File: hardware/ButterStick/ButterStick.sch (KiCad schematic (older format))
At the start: 0 parts

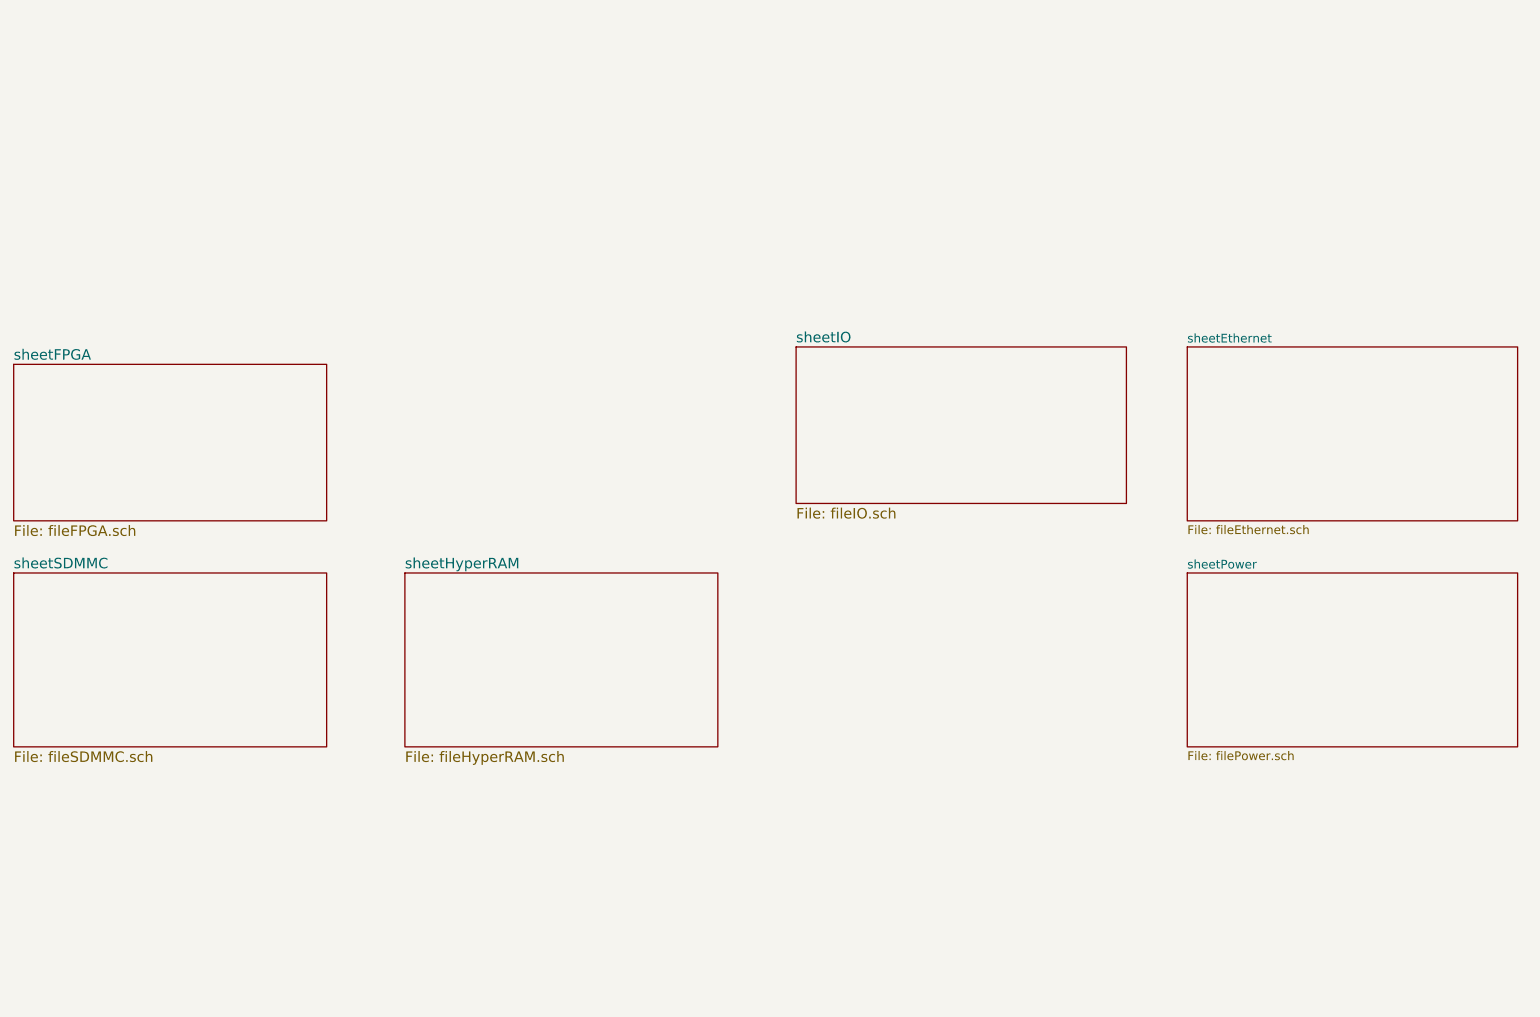
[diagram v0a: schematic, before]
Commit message: Update schematic hieracy layout.
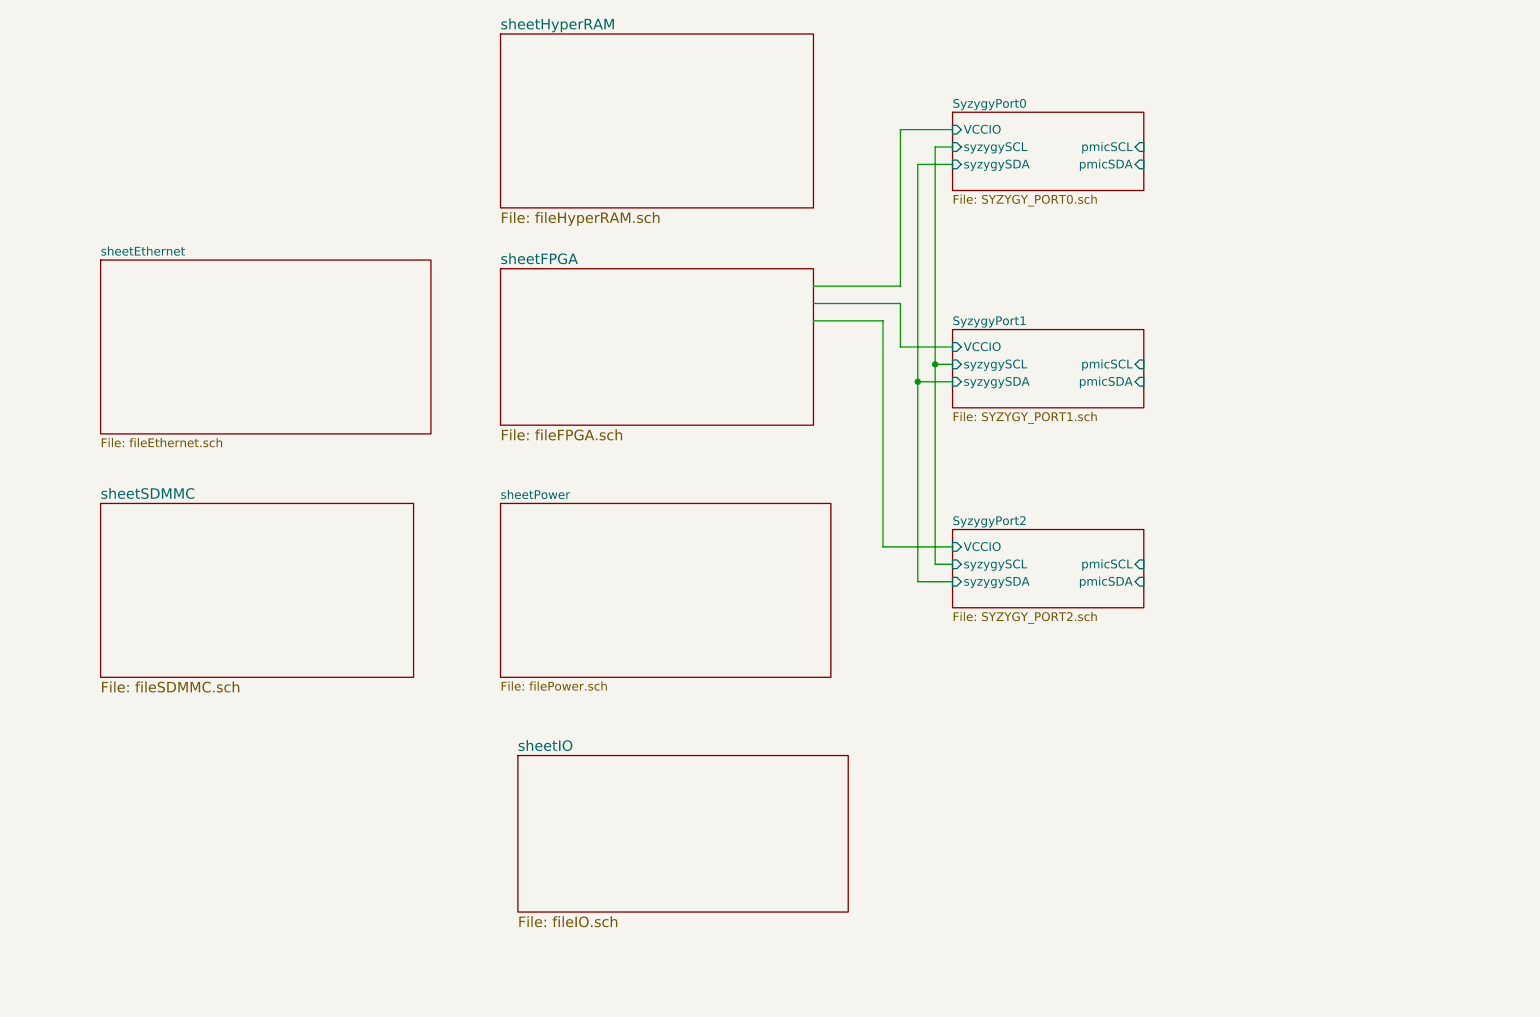
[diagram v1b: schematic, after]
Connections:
- wire segments 0 -> 19
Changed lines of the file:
@@
 $Descr A4 11693 8268
 encoding utf-8
-Sheet 1 7
+Sheet 1 13
 Title ""
 Date ""
@@
 $EndDescr
 $Sheet
-S 1800 3000 1800 900
+S 4600 2450 1800 900
 U 5AB8ACB7
 F0 "sheetFPGA" 60
@@
 $EndSheet
 $Sheet
-S 4050 4200 1800 1000
+S 4600 1100 1800 1000
 U 5ABD38F2
 F0 "sheetHyperRAM" 60
@@
 $EndSheet
 $Sheet
-S 1800 4200 1800 1000
+S 2300 3800 1800 1000
 U 5AC0A2A0
 F0 "sheetSDMMC" 60
@@
 $EndSheet
 $Sheet
-S 6300 2900 1900 900
+S 4700 5250 1900 900
 U 5ABC9A87
 F0 "sheetIO" 60
@@
 $EndSheet
 $Sheet
-S 8550 2900 1900 1000
+S 2300 2400 1900 1000
 U 5BA0BA35
 F0 "sheetEthernet" 50
@@
 $EndSheet
 $Sheet
-S 8550 4200 1900 1000
+S 4600 3800 1900 1000
 U 5BBD18EA
 F0 "sheetPower" 50
 F1 "filePower.sch" 50
 $EndSheet
+$Sheet
+S 7200 1550 1100 450
+U 5C80F19A
+F0 "SyzygyPort0" 50
+F1 "SYZYGY_PORT0.sch" 50
+F2 "VCCIO" I L 7200 1650 50
+F3 "syzygySCL" I L 7200 1750 50
+F4 "syzygySDA" I L 7200 1850 50
+F5 "pmicSCL" I R 8300 1750 50
+F6 "pmicSDA" I R 8300 1850 50
+$EndSheet
+$Sheet
+S 7200 2800 1100 450
+U 5C80F19D
+F0 "SyzygyPort1" 50
+F1 "SYZYGY_PORT1.sch" 50
+F2 "VCCIO" I L 7200 2900 50
+F3 "syzygySCL" I L 7200 3000 50
+F4 "syzygySDA" I L 7200 3100 50
+F5 "pmicSCL" I R 8300 3000 50
+F6 "pmicSDA" I R 8300 3100 50
+$EndSheet
+$Sheet
+S 7200 3950 1100 450
+U 5C80F1A0
+F0 "SyzygyPort2" 50
+F1 "SYZYGY_PORT2.sch" 50
+F2 "VCCIO" I L 7200 4050 50
+F3 "syzygySCL" I L 7200 4150 50
+F4 "syzygySDA" I L 7200 4250 50
+F5 "pmicSCL" I R 8300 4150 50
+F6 "pmicSDA" I R 8300 4250 50
+$EndSheet
+Wire Wire Line
+	7200 4150 7100 4150
+Wire Wire Line
+	7100 4150 7100 3000
+Wire Wire Line
+	7100 1750 7200 1750
+Wire Wire Line
+	7200 1850 7000 1850
+Wire Wire Line
+	7000 1850 7000 3100
+Wire Wire Line
+	7000 4250 7200 4250
+Wire Wire Line
+	7200 3100 7000 3100
+Connection ~ 7000 3100
+Wire Wire Line
+	7000 3100 7000 4250
+Wire Wire Line
+	7200 3000 7100 3000
+Connection ~ 7100 3000
+Wire Wire Line
+	7100 3000 7100 1750
+Wire Wire Line
+	7200 1650 6900 1650
+Wire Wire Line
+	6900 1650 6900 2550
+Wire Wire Line
+	6900 2550 6400 2550
+Wire Wire Line
+	7200 2900 6900 2900
+Wire Wire Line
+	6900 2900 6900 2650
+Wire Wire Line
+	6900 2650 6400 2650
+Wire Wire Line
+	7200 4050 6800 4050
+Wire Wire Line
+	6800 4050 6800 2750
+Wire Wire Line
+	6800 2750 6400 2750
 $EndSCHEMATC

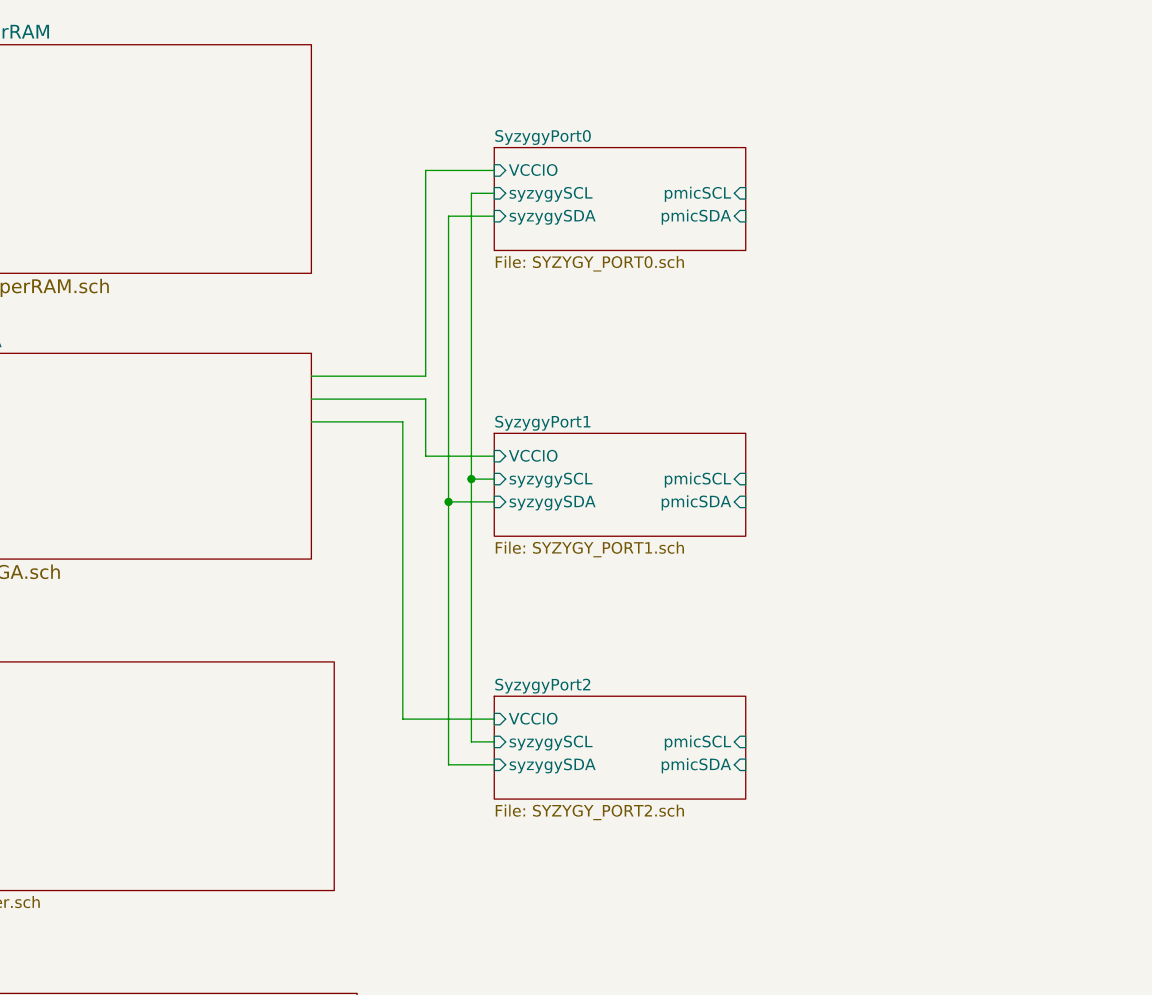
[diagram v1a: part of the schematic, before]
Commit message: Routed all SYZYGY ports. Placed decoupling caps etc.
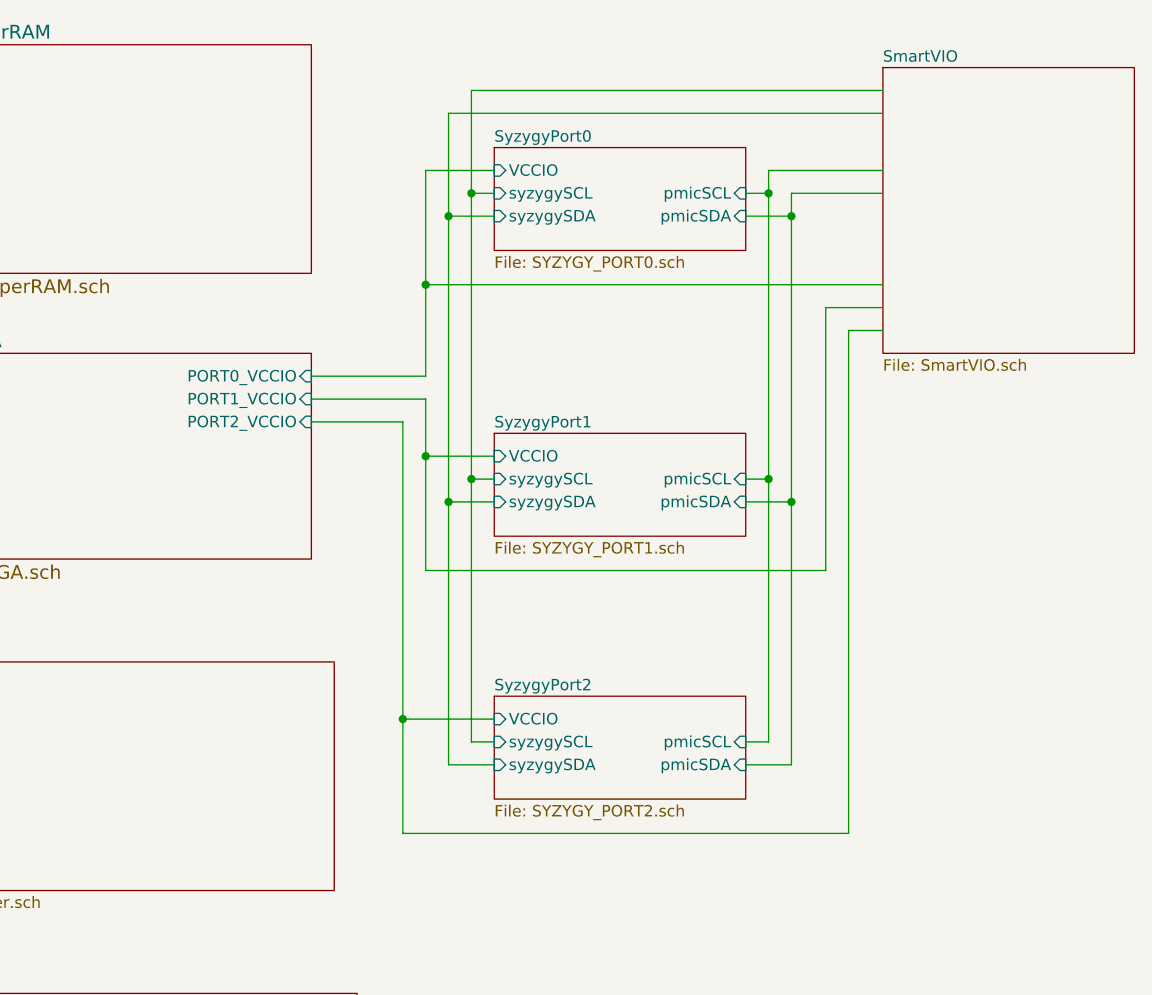
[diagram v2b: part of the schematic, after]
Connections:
- wire segments 19 -> 47
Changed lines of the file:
@@
 $Descr A4 11693 8268
 encoding utf-8
-Sheet 1 13
+Sheet 1 14
 Title ""
 Date ""
@@
 F0 "sheetFPGA" 60
 F1 "fileFPGA.sch" 60
+F2 "PORT0_VCCIO" I R 6400 2550 50
+F3 "PORT1_VCCIO" I R 6400 2650 50
+F4 "PORT2_VCCIO" I R 6400 2750 50
 $EndSheet
 $Sheet
@@
 	7200 1650 6900 1650
 Wire Wire Line
-	6900 1650 6900 2550
+	6900 1650 6900 2150
 Wire Wire Line
 	6900 2550 6400 2550
@@
 Wire Wire Line
 	6800 2750 6400 2750
+$Sheet
+S 8900 1200 1100 1250
+U 5C9D13FE
+F0 "SmartVIO" 50
+F1 "SmartVIO.sch" 50
+$EndSheet
+Wire Wire Line
+	6900 2150 8900 2150
+Connection ~ 6900 2150
+Wire Wire Line
+	6900 2150 6900 2550
+Wire Wire Line
+	6900 2900 6900 3400
+Wire Wire Line
+	6900 3400 8650 3400
+Wire Wire Line
+	8650 3400 8650 2250
+Wire Wire Line
+	8650 2250 8900 2250
+Connection ~ 6900 2900
+Wire Wire Line
+	6800 4050 6800 4550
+Wire Wire Line
+	6800 4550 8750 4550
+Wire Wire Line
+	8750 4550 8750 2350
+Wire Wire Line
+	8750 2350 8900 2350
+Connection ~ 6800 4050
+Wire Wire Line
+	8300 4150 8400 4150
+Wire Wire Line
+	8400 4150 8400 3000
+Wire Wire Line
+	8400 1650 8900 1650
+Wire Wire Line
+	8900 1750 8500 1750
+Wire Wire Line
+	8500 1750 8500 1850
+Wire Wire Line
+	8500 4250 8300 4250
+Wire Wire Line
+	8300 3100 8500 3100
+Connection ~ 8500 3100
+Wire Wire Line
+	8500 3100 8500 4250
+Wire Wire Line
+	8300 3000 8400 3000
+Connection ~ 8400 3000
+Wire Wire Line
+	8400 3000 8400 1750
+Wire Wire Line
+	8300 1850 8500 1850
+Connection ~ 8500 1850
+Wire Wire Line
+	8500 1850 8500 3100
+Wire Wire Line
+	8300 1750 8400 1750
+Connection ~ 8400 1750
+Wire Wire Line
+	8400 1750 8400 1650
+Wire Wire Line
+	7000 1850 7000 1400
+Wire Wire Line
+	7000 1400 8900 1400
+Connection ~ 7000 1850
+Wire Wire Line
+	7100 1750 7100 1300
+Wire Wire Line
+	7100 1300 8900 1300
+Connection ~ 7100 1750
 $EndSCHEMATC

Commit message: Added ESD on SD card signals.
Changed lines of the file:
@@
 $Descr A4 11693 8268
 encoding utf-8
-Sheet 1 14
+Sheet 1 13
 Title ""
 Date ""
@@
 F0 "sheetHyperRAM" 60
 F1 "fileHyperRAM.sch" 60
-$EndSheet
-$Sheet
-S 2300 3800 1800 1000
-U 5AC0A2A0
-F0 "sheetSDMMC" 60
-F1 "fileSDMMC.sch" 60
 $EndSheet
 $Sheet
@@
 F0 "SmartVIO" 50
 F1 "SmartVIO.sch" 50
+F2 "SYZYGY_SDA" I L 8900 1400 50
+F3 "SYZYGY_SCL" I L 8900 1300 50
+F4 "PMIC_SDA" I L 8900 1750 50
+F5 "PMIC_SCL" I L 8900 1650 50
+F6 "SENSE0" I L 8900 2150 50
+F7 "SENSE1" I L 8900 2250 50
+F8 "SENSE2" I L 8900 2350 50
 $EndSheet
 Wire Wire Line

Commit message: Finished initial routing of PCB.. Most parts are finished.
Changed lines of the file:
@@
 F5 "pmicSCL" I R 8300 1750 50
 F6 "pmicSDA" I R 8300 1850 50
+F7 "EN" I R 8300 1650 50
 $EndSheet
 $Sheet
@@
 F5 "pmicSCL" I R 8300 3000 50
 F6 "pmicSDA" I R 8300 3100 50
+F7 "EN" I R 8300 2900 50
 $EndSheet
 $Sheet
@@
 F5 "pmicSCL" I R 8300 4150 50
 F6 "pmicSDA" I R 8300 4250 50
+F7 "EN" I R 8300 4050 50
 $EndSheet
 Wire Wire Line
